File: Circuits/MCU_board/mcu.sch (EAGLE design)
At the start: 74 parts, among them IC1 RP111N331B-TR-FE, IC2 FT230XS, U1 TCA9548APWR, U2 USBLC6-2P6, U4 LSM9DS1, U5 STM32L452RECT6

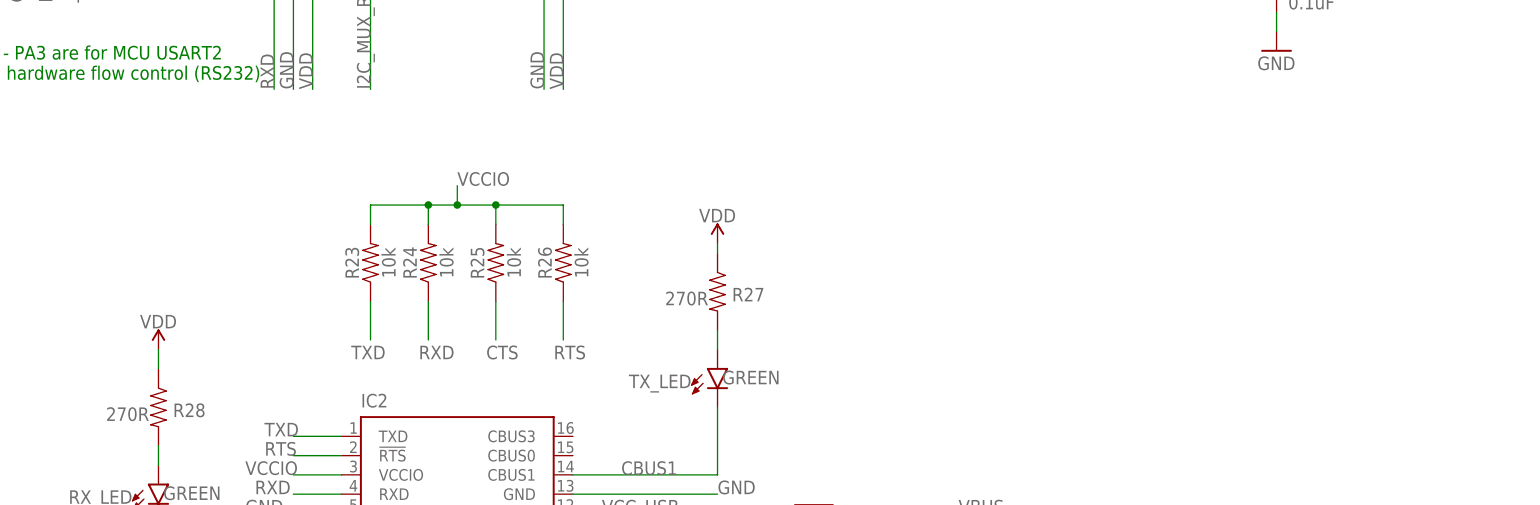
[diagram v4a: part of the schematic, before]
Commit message: Changed routing on FTDI, Added Testpads for each plane, Changed some connector traces
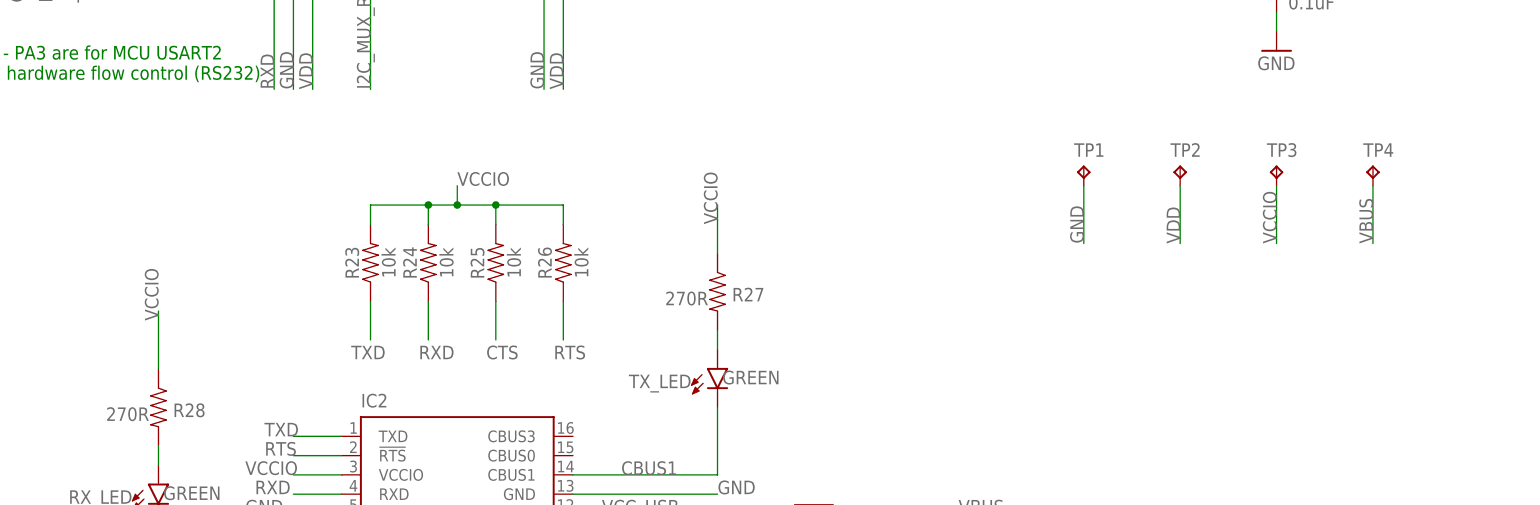
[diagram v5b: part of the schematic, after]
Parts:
- added TP1, TP2, TP3, TP4: TPB2,54, testpad:TPB2,54
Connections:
- net GND: now also TP1.TP
- net VBUS: now also TP4.TP
- net VCCIO: now also R27.1, R28.1, TP3.TP
- net VDD: now also TP2.TP; no longer R27.1, R28.1
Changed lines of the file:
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@@
 <?xml version="1.0" encoding="utf-8"?>
 <!DOCTYPE eagle SYSTEM "eagle.dtd">
-<eagle version="9.3.2">
+<eagle version="9.4.2">
 <drawing>
 <settings>
@@
 <part name="GND27" library="supply1" library_urn="urn:adsk.eagle:library:371" deviceset="GND" device=""/>
 <part name="GND28" library="supply1" library_urn="urn:adsk.eagle:library:371" deviceset="GND" device=""/>
-<part name="SUPPLY24" library="SparkFun-PowerSymbols" deviceset="VDD" device=""/>
 <part name="RX_LED" library="SparkFun-LED" deviceset="LED-GREEN" device="0603" value="GREEN"/>
 <part name="R28" library="SparkFun-Resistors" deviceset="4.7KOHM" device="-0603-1/10W-1%" value="270R"/>
-<part name="SUPPLY25" library="SparkFun-PowerSymbols" deviceset="VDD" device=""/>
 <part name="GND29" library="supply1" library_urn="urn:adsk.eagle:library:371" deviceset="GND" device=""/>
 <part name="GND30" library="supply1" library_urn="urn:adsk.eagle:library:371" deviceset="GND" device=""/>
@@
 <part name="SUPPLY26" library="SparkFun-PowerSymbols" deviceset="VDD" device=""/>
 <part name="SUPPLY27" library="SparkFun-PowerSymbols" deviceset="VDD" device=""/>
+<part name="TP1" library="testpad" library_urn="urn:adsk.eagle:library:385" deviceset="TP" device="B2,54" package3d_urn="urn:adsk.eagle:package:27948/1"/>
+<part name="TP2" library="testpad" library_urn="urn:adsk.eagle:library:385" deviceset="TP" device="B2,54" package3d_urn="urn:adsk.eagle:package:27948/1"/>
+<part name="TP3" library="testpad" library_urn="urn:adsk.eagle:library:385" deviceset="TP" device="B2,54" package3d_urn="urn:adsk.eagle:package:27948/1"/>
+<part name="TP4" library="testpad" library_urn="urn:adsk.eagle:library:385" deviceset="TP" device="B2,54" package3d_urn="urn:adsk.eagle:package:27948/1"/>
 </parts>
 <sheets>
@@
 <attribute name="VALUE" x="54.61" y="-50.8" size="1.778" layer="96"/>
 </instance>
-<instance part="SUPPLY24" gate="VDD" x="127" y="10.16" smashed="yes">
-<attribute name="VALUE" x="127" y="12.954" size="1.778" layer="96" align="bottom-center"/>
-</instance>
 <instance part="RX_LED" gate="G$1" x="53.34" y="-21.59" smashed="yes">
 <attribute name="NAME" x="49.911" y="-22.352" size="1.778" layer="95" font="vector" rot="R180"/>
@@
 <attribute name="VALUE" x="49.276" y="-11.43" size="1.778" layer="96" font="vector" align="top-center"/>
 </instance>
-<instance part="SUPPLY25" gate="VDD" x="53.34" y="-3.81" smashed="yes">
-<attribute name="VALUE" x="53.34" y="-1.016" size="1.778" layer="96" align="bottom-center"/>
-</instance>
 <instance part="GND29" gate="1" x="111.76" y="-59.69" smashed="yes">
 <attribute name="VALUE" x="109.22" y="-62.23" size="1.778" layer="96"/>
@@
 <instance part="SUPPLY27" gate="VDD" x="-223.52" y="129.54" smashed="yes">
 <attribute name="VALUE" x="-223.52" y="132.334" size="1.778" layer="96" align="bottom-center"/>
+</instance>
+<instance part="TP1" gate="G$1" x="175.26" y="20.32" smashed="yes">
+<attribute name="NAME" x="173.99" y="21.59" size="1.778" layer="95"/>
+<attribute name="TP_SIGNAL_NAME" x="176.53" y="19.05" size="1.778" layer="97"/>
+</instance>
+<instance part="TP2" gate="G$1" x="187.96" y="20.32" smashed="yes">
+<attribute name="NAME" x="186.69" y="21.59" size="1.778" layer="95"/>
+<attribute name="TP_SIGNAL_NAME" x="189.23" y="19.05" size="1.778" layer="97"/>
+</instance>
+<instance part="TP3" gate="G$1" x="200.66" y="20.32" smashed="yes">
+<attribute name="NAME" x="199.39" y="21.59" size="1.778" layer="95"/>
+<attribute name="TP_SIGNAL_NAME" x="201.93" y="19.05" size="1.778" layer="97"/>
+</instance>
+<instance part="TP4" gate="G$1" x="213.36" y="20.32" smashed="yes">
+<attribute name="NAME" x="212.09" y="21.59" size="1.778" layer="95"/>
+<attribute name="TP_SIGNAL_NAME" x="214.63" y="19.05" size="1.778" layer="97"/>
 </instance>
 </instances>
@@
 <wire x1="-93.98" y1="81.28" x2="-93.98" y2="63.5" width="0.1524" layer="91"/>
 <label x="-93.98" y="63.5" size="1.778" layer="95" rot="R90"/>
+</segment>
+<segment>
+<pinref part="TP1" gate="G$1" pin="TP"/>
+<wire x1="175.26" y1="17.78" x2="175.26" y2="10.16" width="0.1524" layer="91"/>
+<label x="175.26" y="10.16" size="1.778" layer="95" rot="R90"/>
 </segment>
 </net>
@@
 </segment>
 <segment>
-<pinref part="SUPPLY24" gate="VDD" pin="VDD"/>
-<pinref part="R27" gate="G$1" pin="1"/>
-<wire x1="127" y1="10.16" x2="127" y2="8.89" width="0.1524" layer="91"/>
-</segment>
-<segment>
-<pinref part="SUPPLY25" gate="VDD" pin="VDD"/>
-<pinref part="R28" gate="G$1" pin="1"/>
-<wire x1="53.34" y1="-3.81" x2="53.34" y2="-6.35" width="0.1524" layer="91"/>
-</segment>
-<segment>
 <pinref part="U$1" gate="G$1" pin="4"/>
 <wire x1="-213.36" y1="81.28" x2="-213.36" y2="63.5" width="0.1524" layer="91"/>
@@
 <wire x1="-223.52" y1="124.46" x2="-223.52" y2="129.54" width="0.1524" layer="91"/>
 <pinref part="SUPPLY27" gate="VDD" pin="VDD"/>
+</segment>
+<segment>
+<pinref part="TP2" gate="G$1" pin="TP"/>
+<wire x1="187.96" y1="17.78" x2="187.96" y2="10.16" width="0.1524" layer="91"/>
+<label x="187.96" y="10.16" size="1.778" layer="95" rot="R90"/>
 </segment>
 </net>
@@
 <wire x1="153.67" y1="-25.4" x2="158.75" y2="-25.4" width="0.1524" layer="91"/>
 <label x="158.75" y="-25.4" size="1.778" layer="95"/>
+</segment>
+<segment>
+<pinref part="TP4" gate="G$1" pin="TP"/>
+<wire x1="213.36" y1="17.78" x2="213.36" y2="10.16" width="0.1524" layer="91"/>
+<label x="213.36" y="10.16" size="1.778" layer="95" rot="R90"/>
 </segment>
 </net>
@@
 <pinref part="R26" gate="G$1" pin="2"/>
 </segment>
-</net>
+<segment>
+<pinref part="R28" gate="G$1" pin="1"/>
+<wire x1="53.34" y1="1.27" x2="53.34" y2="-6.35" width="0.1524" layer="91"/>
+<label x="53.34" y="0" size="1.778" layer="95" rot="R90"/>
+</segment>
+<segment>
+<pinref part="R27" gate="G$1" pin="1"/>
+<wire x1="127" y1="15.24" x2="127" y2="8.89" width="0.1524" layer="91"/>
+<label x="127" y="12.7" size="1.778" layer="95" rot="R90"/>
+</segment>
+<segment>
+<pinref part="TP3" gate="G$1" pin="TP"/>
+<wire x1="200.66" y1="17.78" x2="200.66" y2="10.16" width="0.1524" layer="91"/>
+<label x="200.66" y="10.16" size="1.778" layer="95" rot="R90"/>
+</segment>
+</net>

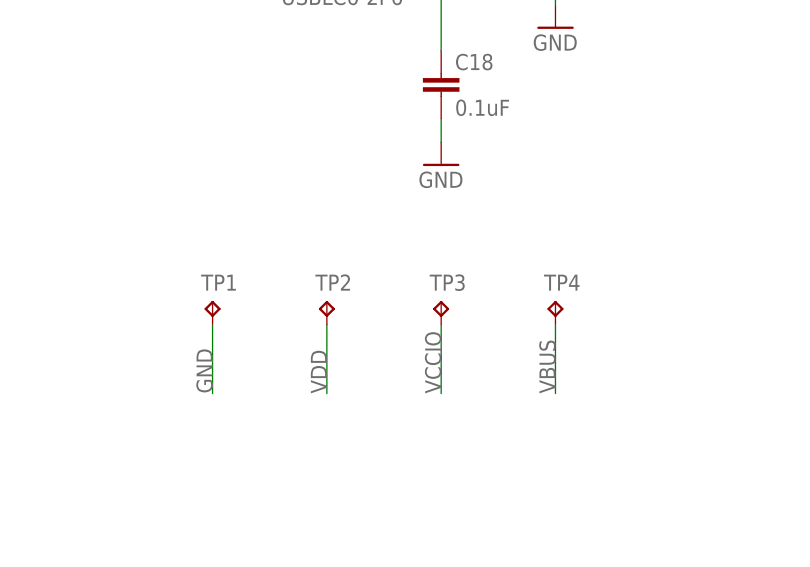
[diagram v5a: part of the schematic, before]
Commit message: Fixed silkscreen of components, Changed VCCIO plane
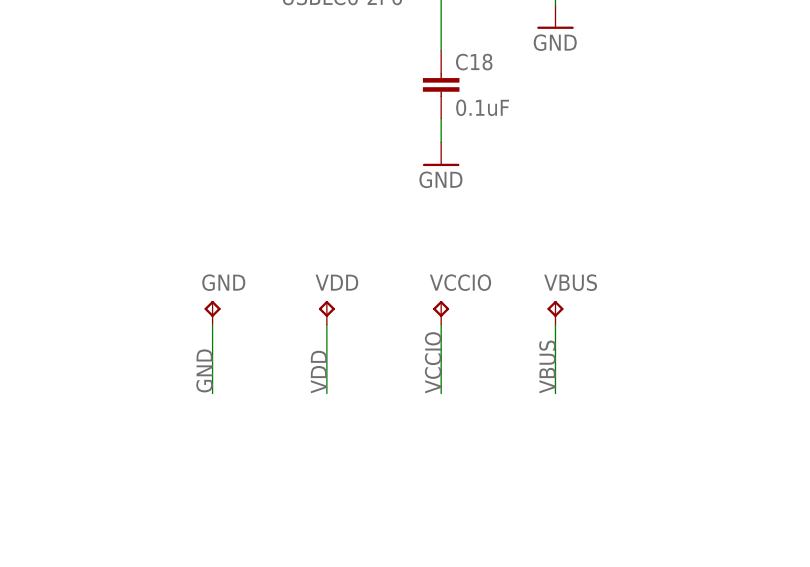
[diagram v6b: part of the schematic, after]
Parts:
- renumbered TP1 to GND, TP2 to VDD, TP3 to VCCIO, TP4 to VBUS
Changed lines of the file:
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@@
 <part name="SUPPLY26" library="SparkFun-PowerSymbols" deviceset="VDD" device=""/>
 <part name="SUPPLY27" library="SparkFun-PowerSymbols" deviceset="VDD" device=""/>
-<part name="TP1" library="testpad" library_urn="urn:adsk.eagle:library:385" deviceset="TP" device="B2,54" package3d_urn="urn:adsk.eagle:package:27948/1"/>
-<part name="TP2" library="testpad" library_urn="urn:adsk.eagle:library:385" deviceset="TP" device="B2,54" package3d_urn="urn:adsk.eagle:package:27948/1"/>
-<part name="TP3" library="testpad" library_urn="urn:adsk.eagle:library:385" deviceset="TP" device="B2,54" package3d_urn="urn:adsk.eagle:package:27948/1"/>
-<part name="TP4" library="testpad" library_urn="urn:adsk.eagle:library:385" deviceset="TP" device="B2,54" package3d_urn="urn:adsk.eagle:package:27948/1"/>
+<part name="GND" library="testpad" library_urn="urn:adsk.eagle:library:385" deviceset="TP" device="B2,54" package3d_urn="urn:adsk.eagle:package:27948/1"/>
+<part name="VDD" library="testpad" library_urn="urn:adsk.eagle:library:385" deviceset="TP" device="B2,54" package3d_urn="urn:adsk.eagle:package:27948/1"/>
+<part name="VCCIO" library="testpad" library_urn="urn:adsk.eagle:library:385" deviceset="TP" device="B2,54" package3d_urn="urn:adsk.eagle:package:27948/1"/>
+<part name="VBUS" library="testpad" library_urn="urn:adsk.eagle:library:385" deviceset="TP" device="B2,54" package3d_urn="urn:adsk.eagle:package:27948/1"/>
 </parts>
 <sheets>
@@
 <attribute name="VALUE" x="-223.52" y="132.334" size="1.778" layer="96" align="bottom-center"/>
 </instance>
-<instance part="TP1" gate="G$1" x="175.26" y="20.32" smashed="yes">
+<instance part="GND" gate="G$1" x="175.26" y="20.32" smashed="yes">
 <attribute name="NAME" x="173.99" y="21.59" size="1.778" layer="95"/>
 <attribute name="TP_SIGNAL_NAME" x="176.53" y="19.05" size="1.778" layer="97"/>
 </instance>
-<instance part="TP2" gate="G$1" x="187.96" y="20.32" smashed="yes">
+<instance part="VDD" gate="G$1" x="187.96" y="20.32" smashed="yes">
 <attribute name="NAME" x="186.69" y="21.59" size="1.778" layer="95"/>
 <attribute name="TP_SIGNAL_NAME" x="189.23" y="19.05" size="1.778" layer="97"/>
 </instance>
-<instance part="TP3" gate="G$1" x="200.66" y="20.32" smashed="yes">
+<instance part="VCCIO" gate="G$1" x="200.66" y="20.32" smashed="yes">
 <attribute name="NAME" x="199.39" y="21.59" size="1.778" layer="95"/>
 <attribute name="TP_SIGNAL_NAME" x="201.93" y="19.05" size="1.778" layer="97"/>
 </instance>
-<instance part="TP4" gate="G$1" x="213.36" y="20.32" smashed="yes">
+<instance part="VBUS" gate="G$1" x="213.36" y="20.32" smashed="yes">
 <attribute name="NAME" x="212.09" y="21.59" size="1.778" layer="95"/>
 <attribute name="TP_SIGNAL_NAME" x="214.63" y="19.05" size="1.778" layer="97"/>
@@
 </segment>
 <segment>
-<pinref part="TP1" gate="G$1" pin="TP"/>
+<pinref part="GND" gate="G$1" pin="TP"/>
 <wire x1="175.26" y1="17.78" x2="175.26" y2="10.16" width="0.1524" layer="91"/>
 <label x="175.26" y="10.16" size="1.778" layer="95" rot="R90"/>
@@
 </segment>
 <segment>
-<pinref part="TP2" gate="G$1" pin="TP"/>
+<pinref part="VDD" gate="G$1" pin="TP"/>
 <wire x1="187.96" y1="17.78" x2="187.96" y2="10.16" width="0.1524" layer="91"/>
 <label x="187.96" y="10.16" size="1.778" layer="95" rot="R90"/>
@@
 </segment>
 <segment>
-<pinref part="TP4" gate="G$1" pin="TP"/>
+<pinref part="VBUS" gate="G$1" pin="TP"/>
 <wire x1="213.36" y1="17.78" x2="213.36" y2="10.16" width="0.1524" layer="91"/>
 <label x="213.36" y="10.16" size="1.778" layer="95" rot="R90"/>
@@
 </segment>
 <segment>
-<pinref part="TP3" gate="G$1" pin="TP"/>
+<pinref part="VCCIO" gate="G$1" pin="TP"/>
 <wire x1="200.66" y1="17.78" x2="200.66" y2="10.16" width="0.1524" layer="91"/>
 <label x="200.66" y="10.16" size="1.778" layer="95" rot="R90"/>
